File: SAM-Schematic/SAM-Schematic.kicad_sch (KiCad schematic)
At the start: 1 part

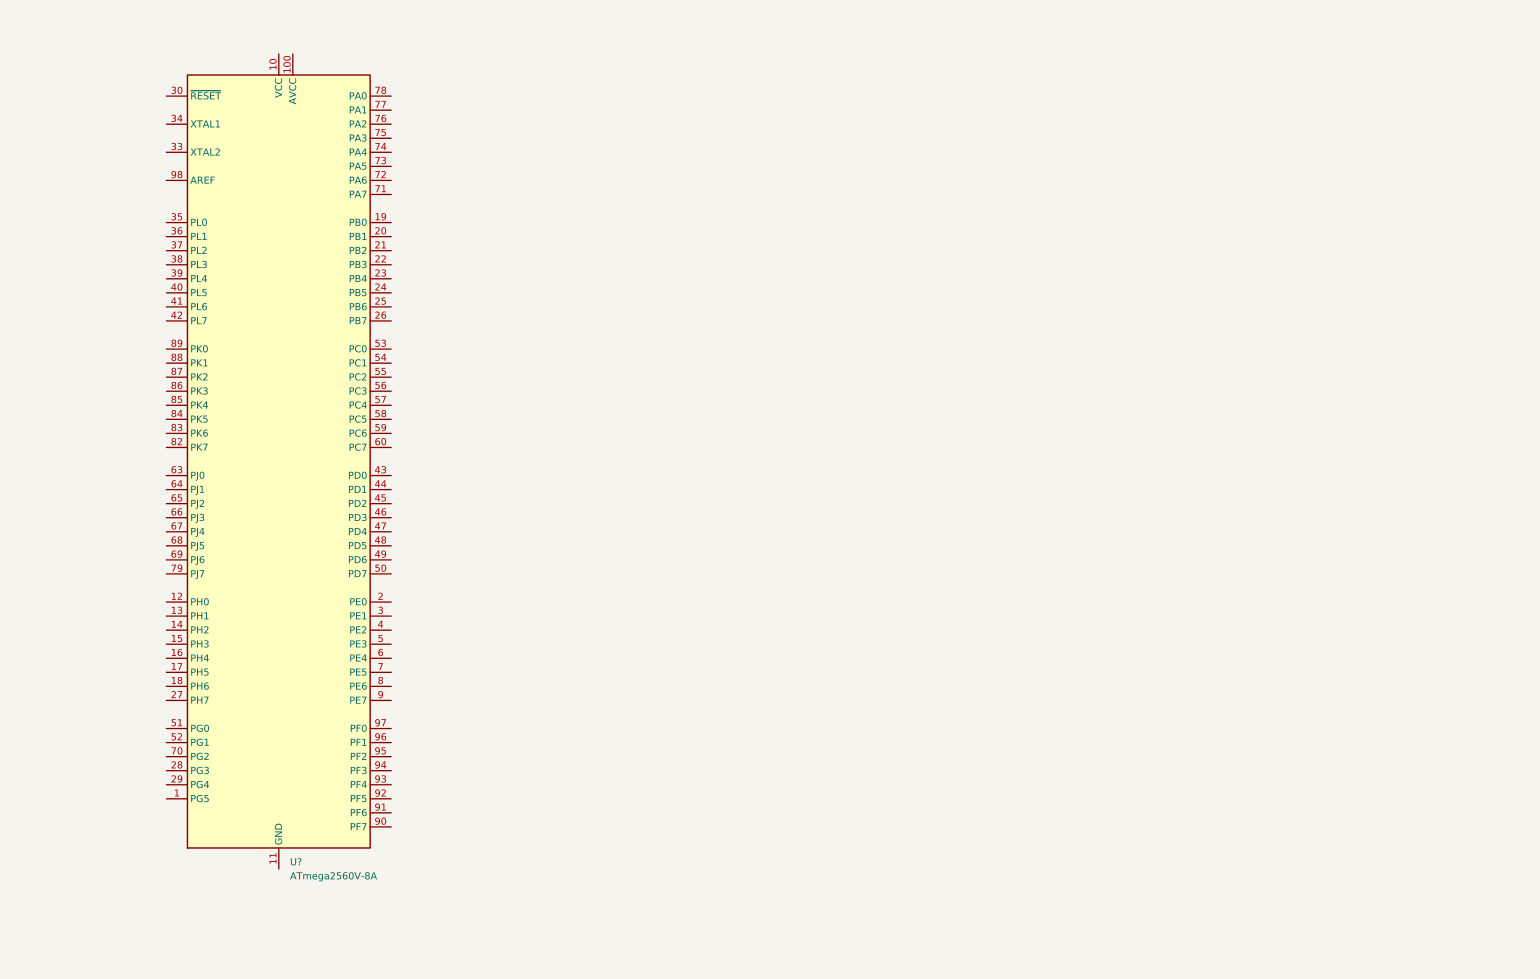
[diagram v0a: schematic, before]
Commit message: chm first draft
need to update relay names and may need to change arduino pins. Assumed we'd use I2C for LCD screen but we could do it the beefy pin way too
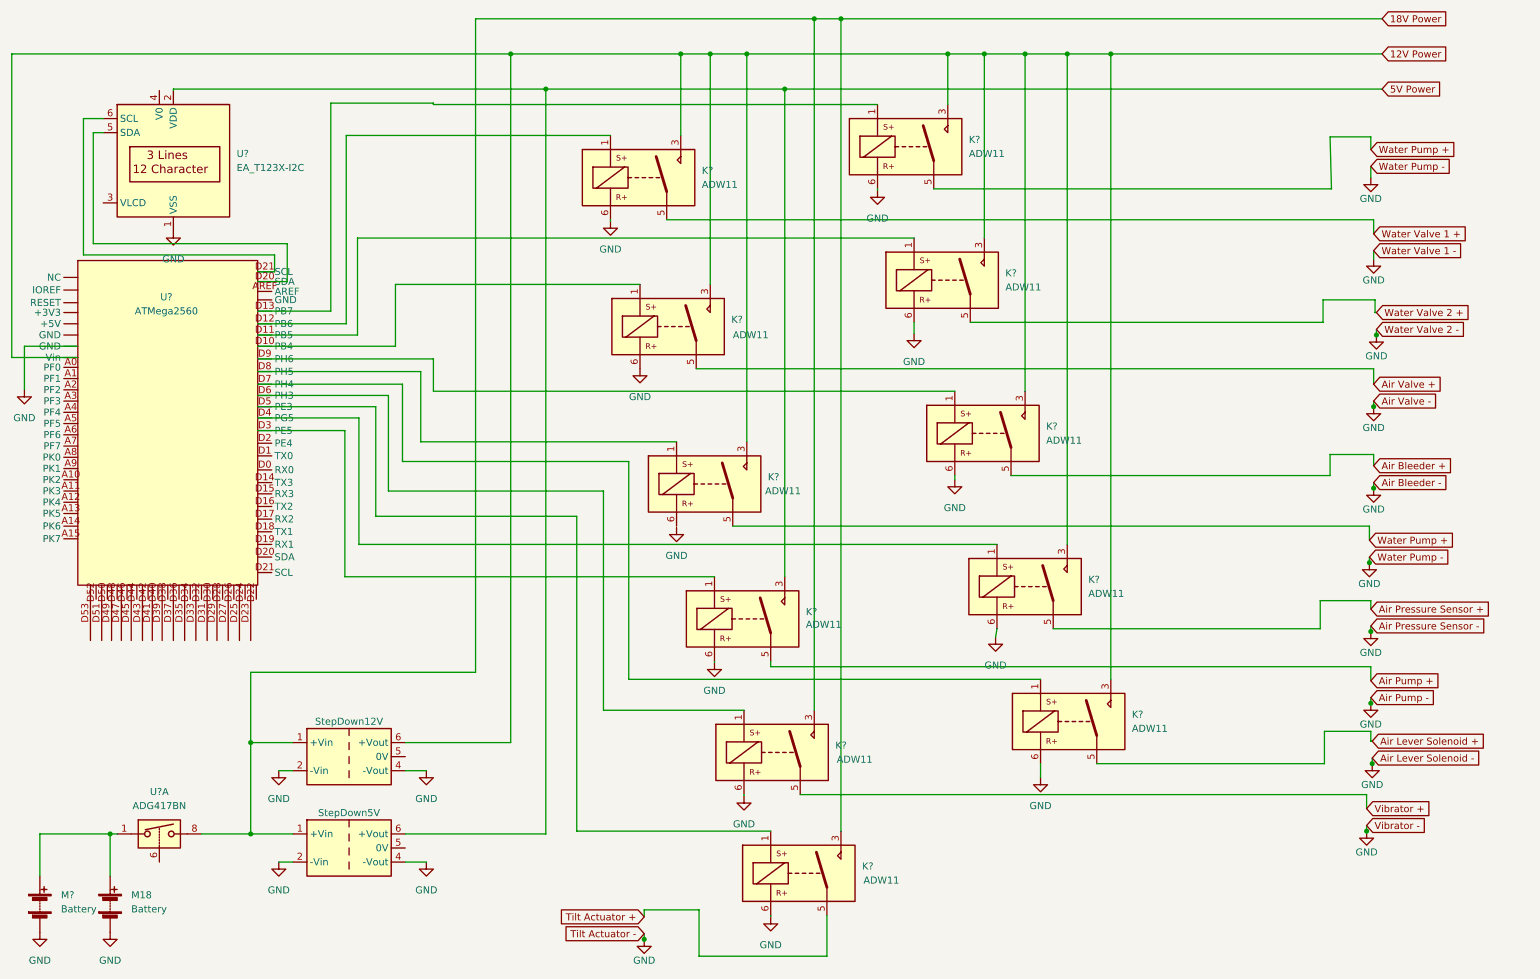
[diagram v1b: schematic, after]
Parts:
- removed U?: ATmega2560V-8A, Package_QFP:TQFP-100_14x14mm_P0.5mm, symbol MCU_Microchip_ATmega:ATmega2560V-8A
- added K? (x11): ADW11, Relay_THT:Relay_1P1T_NO_10x24x18.8mm_Panasonic_ADW11xxxxW_THT, symbol Relay:ADW11
- added M18, M?: Battery, symbol Device:Battery
- added PS?: StepDown12V, Converter_DCDC:Converter_DCDC_XP_POWER-IHxxxxSH_THT, symbol Converter_DCDC:IH2409SH
- added Ps?: StepDown5V, Converter_DCDC:Converter_DCDC_XP_POWER-IHxxxxSH_THT, symbol Converter_DCDC:IH2409SH
- added U?: EA_T123X-I2C, Display:EA_T123X-I2C, symbol Display_Character:EA_T123X-I2C
- added U?: ADG417BN, Package_DIP:DIP-8_W7.62mm, symbol Analog_Switch:ADG417BN
- added U?: ATMega2560, symbol ECEN4024SAM:ATMega2560
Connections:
- new net: M18.1 (+), M?.1 (+), U?.1
- new net: U?.5 (SDA), U?.D20 (SDA)
- new net: U?.6 (SCL), U?.D21 (SCL)
- new net: K?.1, U?.D13 (PB7)
- new net: K?.1, U?.D3 (PE5)
- new net: K?.1, U?.D6 (PH3)
- new net: K?.1, U?.D4 (PG5)
- new net: K?.1, U?.D12 (PB6)
- new net: K?.1, U?.D11 (PB5)
- new net: K?.1, U?.D5 (PE3)
- new net: K?.1, U?.D7 (PH4)
- new net: K?.1, U?.D8 (PH5)
- new net: K?.1, U?.D10 (PB4)
- new net: K?.1, U?.D9 (PH6)
- new net 12V Power: K?.3, K?.3, K?.3, K?.3, K?.3, K?.3, K?.3, K?.3, PS?.6 (+Vout), U?. (Vin)
- new net 18V Power: K?.3, K?.3, PS?.1 (+Vin), Ps?.1 (+Vin), U?.8
- new net 5V Power: K?.3, Ps?.6 (+Vout), U?.2 (VDD)
- new net Air Bleeder +: K?.5
- new net Air Lever Solenoid +: K?.5
- new net Air Pressure Sensor +: K?.5
- new net Air Pump +: K?.5
- new net Air Valve +: K?.5
- new net GND: K?.6, K?.6, K?.6, K?.6, K?.6, K?.6, K?.6, K?.6, K?.6, K?.6, M18.2 (-), M?.2 (-), PS?.2 (-Vin), PS?.4 (-Vout), Ps?.2 (-Vin), Ps?.4 (-Vout), U?. (Vin), U?.1 (VSS)
- new net Tilt Actuator +: K?.5
- new net Vibrator +: K?.5
- new net Water Pump +: K?.5, K?.5
- new net Water Valve 1 +: K?.5
- new net Water Valve 2 +: K?.5

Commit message: Cleaned up a bit
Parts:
- removed U?: ADG417BN, Package_DIP:DIP-8_W7.62mm, symbol Analog_Switch:ADG417BN
- added SW?: Master On/Off Switch, symbol Switch:SW_Push_Dual_x2
- added SW?: Start Button, symbol Switch:SW_Push_Dual_x2
- K? (x11): value ADW11 -> Relay
- U?: value EA_T123X-I2C -> LCD Screen
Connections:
- net 18V Power: now also SW?.2 (D)
- net GND: now also SW?.3 (C)
- net at M18.1 (+), M?.1 (+): now also SW?.1 (C)
- net at U?.D2 (PE4): now also SW?.4 (D)

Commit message: schematic update
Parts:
- removed K?: Relay, Relay_THT:Relay_1P1T_NO_10x24x18.8mm_Panasonic_ADW11xxxxW_THT, symbol Relay:ADW11
- removed M18, M?: Battery, symbol Device:Battery
- removed PS?: StepDown12V, Converter_DCDC:Converter_DCDC_XP_POWER-IHxxxxSH_THT, symbol Converter_DCDC:IH2409SH
- removed Ps?: StepDown5V, Converter_DCDC:Converter_DCDC_XP_POWER-IHxxxxSH_THT, symbol Converter_DCDC:IH2409SH
- removed SW?: Master On/Off Switch, symbol Switch:SW_Push_Dual_x2
- removed SW?: Start Button, symbol Switch:SW_Push_Dual_x2
- removed U?: LCD Screen, Display:EA_T123X-I2C, symbol Display_Character:EA_T123X-I2C
- added 10k (x2): R, symbol Device:R
- added M? (x2): Battery, symbol Device:Battery
- added PS?: StepDown12V, Converter_DCDC:Converter_DCDC_XP_POWER-IHxxxxSH_THT, symbol Converter_DCDC:IH2409SH
- added Ps?: StepDown5V, Converter_DCDC:Converter_DCDC_XP_POWER-IHxxxxSH_THT, symbol Converter_DCDC:IH2409SH
- added SW?: Start Button, symbol Switch:SW_Push_Dual_x2
- added SW?: Master On/Off Switch, symbol Switch:SW_Push_Dual_x2
- added SW?: Vibrate Button, symbol Switch:SW_Push_Dual_x2
- added U?: LCD Screen, Display:EA_T123X-I2C, symbol Display_Character:EA_T123X-I2C
- added USB: CH340E, Package_SO:MSOP-10_3x3mm_P0.5mm, symbol Interface_USB:CH340E
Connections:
- net 12V Power: now also PS?.6 (+Vout); no longer U?. (Vin)
- net 18V Power: now also PS?.1 (+Vin), Ps?.1 (+Vin), SW?.2 (D)
- net 5V Power: now also U?. (Vin), Ps?.6 (+Vout), SW?.4 (D), SW?.4 (D), U?.2 (VDD), USB.7 (VCC)
- net GND: now also 10k.2, 10k.2, M?.2 (-), M?.2 (-), PS?.2 (-Vin), PS?.4 (-Vout), Ps?.2 (-Vin), Ps?.4 (-Vout), U?.1 (VSS), USB.3 (GND)
- net Water Pump +: no longer K?.5
- net at U?.D2 (PE4): now also 10k.1, SW?.3 (C)
- net at U?.D1 (TX0): now also 10k.1, SW?.3 (C)
- net at U?.D22: now also USB.8 (TXD)
- net at U?.D23: now also USB.9 (RXD)
- net Air Pressure Sensor + renamed Air Transducer +
- new net: M?.1 (+), M?.1 (+), SW?.1 (C)
- new net: U?.5 (SDA), U?.D20 (SDA)
- new net: U?.6 (SCL), U?.D21 (SCL)
- new net Rocker Actuator +: K?.5
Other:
- moved on the sheet: U?
